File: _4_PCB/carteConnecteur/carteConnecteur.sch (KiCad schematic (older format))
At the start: 15 parts, among them P1 +5 (ubec), P10 N.U, P11 I2c, P2 PAP_D, P3 +5 (pap_G), P4 +5 (pap_D), P5 PAP_G, P6 RPi_Conn, P7 +5 (sonar), P8 +5 (RPi)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

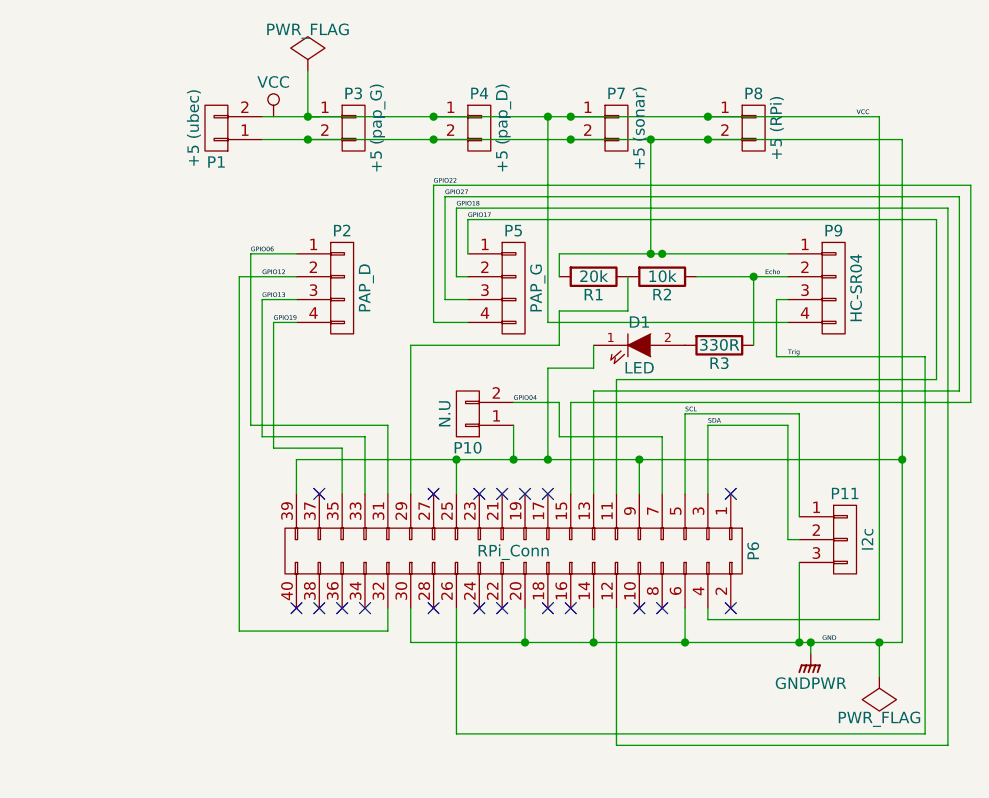
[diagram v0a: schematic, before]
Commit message: ajout de 3 connecteur + pull-up sur le PCB + mise à jour des libs dans 'software'
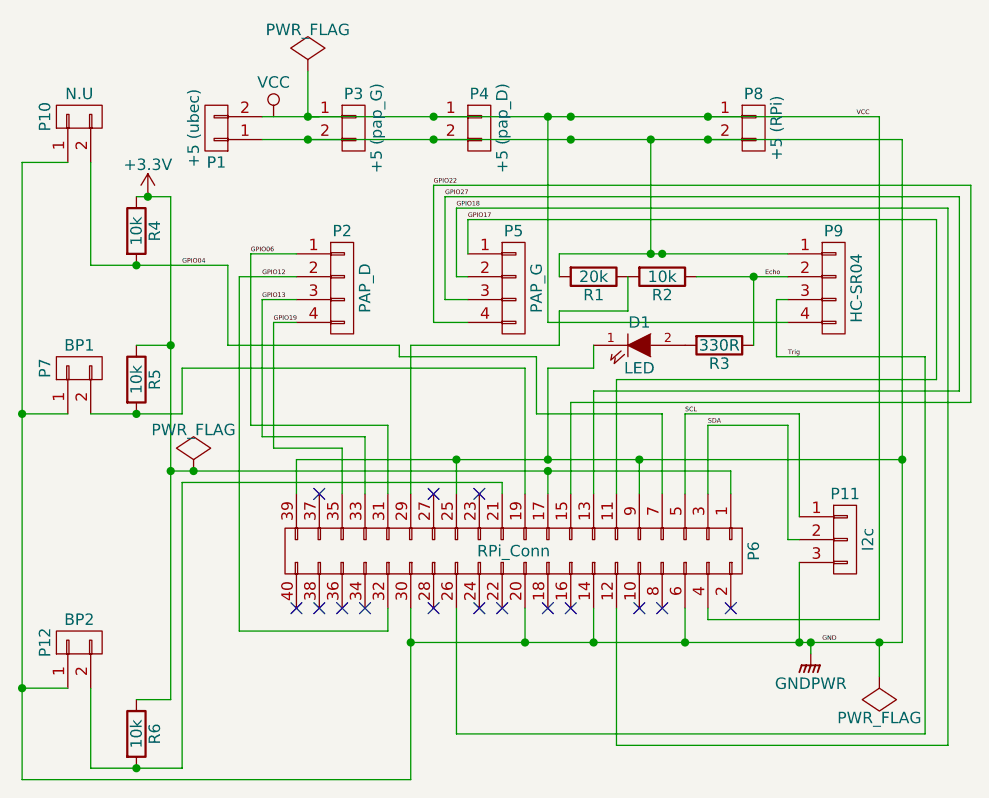
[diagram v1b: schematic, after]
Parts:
- added P12: BP2, Pin_Headers:Pin_Header_Straight_1x02, symbol CONN_01X02
- added R4, R5, R6: 10k, myLib:Resistor_Vertical_2-54, symbol R
- P7: value +5 (sonar) -> BP1; footprint XH_connector:XH_connector_2pins_Vert -> Pin_Headers:Pin_Header_Straight_1x02
- R1, R2, R3: footprint Resistors_ThroughHole:Resistor_Vertical_RM5mm -> myLib:Resistor_Vertical_2-54
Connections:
- net GNDPWR: now also P7.1 (P1), P12.1 (P1); no longer P7.2 (P2)
- net GPIO04: now also R4.2
- net VCC: no longer P7.1 (P1)
- net +3V3: now reaches P6.1 (P1)
- net +3V3: now also P6.17 (P17), R4.1, R5.1, R6.1
- net at P6.19 (P19): now also P7.2 (P2), R5.2
- net at P6.21 (P21): now also P12.2 (P2), R6.2
- no-connect marks 19 -> 15
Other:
- moved on the sheet: P10
